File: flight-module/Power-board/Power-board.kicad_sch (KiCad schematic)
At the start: 22 parts, among them J1 POWER, J3 XT60-M, J5 POWER, J8 XT60-M, U1 AZ1117IH-3.3TRG1, U4 AZ1117IH-5TRG1

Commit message: Added a gpio expander to power board.
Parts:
- added J2, J4, J6: Conn_01x02_Male, Connector_PinHeader_2.54mm:PinHeader_1x02_P2.54mm_Vertical, symbol Connector:Conn_01x02_Male
- added R21, R22, R23: 10k, Resistor_SMD:R_0603_1608Metric, symbol Device:R_Small
- added U2: PCF8575DW, PCF8575DW:SOIC127P1030X265-24N, symbol PCF8575DW:PCF8575DW
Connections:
- net +5V: now also U2.24 (VCC)
- net 3.3V: now also J2.1 (Pin_1), J4.1 (Pin_1), J6.1 (Pin_1)
- net GND: now also R21.1, R22.1, R23.1, U2.12 (GND)
- new net: J2.2 (Pin_2), R21.2, U2.2 (A1)
- new net: J4.2 (Pin_2), R22.2, U2.3 (A2)
- new net: J6.2 (Pin_2), R23.2, U2.21 (A0)
- new net I2C_SCL: U2.22 (SCL)
- new net I2C_SDA: U2.23 (SDA)
- new net PYRO10EN: U2.7 (P03)
- new net PYRO1EN: U2.13 (P10)
- new net PYRO2EN: U2.11 (P07)
- new net PYRO3EN: U2.14 (P11)
- new net PYRO4EN: U2.10 (P06)
- new net PYRO5EN: U2.15 (P12)
- new net PYRO6EN: U2.9 (P05)
- new net PYRO7EN: U2.16 (P13)
- new net PYRO8EN: U2.8 (P04)
- new net PYRO9EN: U2.17 (P14)
- no-connect marks 2 -> 9
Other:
- note added: "Connect to LiPo Battery"
- note removed: "Connect to Battery/ Power Supply"
- moved on the sheet: J?A, J?B

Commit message: power board updated
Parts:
- added C8, C9: 22 µF, symbol Device:C
- added D17, D18, D19, D20: D_Schottky, symbol Device:D_Schottky
- added R24, R26: R, symbol Device:R
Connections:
- net 3.3V is gone; now on net +3.3V: C1.2, F2.2, J2.1 (Pin_1), J4.1 (Pin_1), J6.1 (Pin_1)
- net 5V is gone; now on net +5V: C3.2, F3.2
- net BAT2_- is gone; now on net GND2: C4.1, D1.2 (A), J1.2 (Pin_2), J3.N (NEG)
- net +3.3V: now also J?.A1 (Pin_1), J?.A2 (Pin_2)
- net +5V: now also J?.A5 (Pin_5), J?.A6 (Pin_6), J?.A7 (Pin_7), J?.A8 (Pin_8)
- net BAT2_+: now also D19.2 (A)
- net GND2: now reaches J?.A10 (Pin_10)
- net GND2: now also J?.A13 (Pin_13), J?.A14 (Pin_14), J?.A17 (Pin_17), J?.A18 (Pin_18), J?.A21 (Pin_21), J?.A22 (Pin_22), J?.A25 (Pin_25), J?.A26 (Pin_26), J?.A3 (Pin_3), J?.A33 (Pin_33), J?.A34 (Pin_34), J?.A4 (Pin_4), J?.A9 (Pin_9)
- net LOX_Vent: now reaches J?.A11 (Pin_11)
- net LOX_Vent: now also J?.A12 (Pin_12)
- net ETH_Vent: now reaches J?.A15 (Pin_15)
- net ETH_Vent: now also J?.A16 (Pin_16)
- net ETH_Main: now reaches J?.A19 (Pin_19)
- net ETH_Main: now also J?.A20 (Pin_20)
- net PYRO_EX: now reaches J?.A23 (Pin_23)
- net PYRO_EX: now also J?.A24 (Pin_24)
- net Ext_Sup1: now reaches J?.A27 (Pin_27)
- net Ext_Sup1: now also J?.A28 (Pin_28), J?.A29 (Pin_29), J?.A30 (Pin_30), J?.A31 (Pin_31), J?.A32 (Pin_32), D17.2 (A)
- net Ext_Sup2: now reaches J?.A35 (Pin_35)
- net Ext_Sup2: now also J?.A36 (Pin_36), J?.A37 (Pin_37), J?.A38 (Pin_38), J?.A39 (Pin_39), J?.A40 (Pin_40), D20.2 (A)
- net 12V renamed V_sensor_+
- net V_sensor_+: now also D18.1 (K), R26.2; no longer F1.2
- net PYRO10EN: no longer names the net of U2.7 (P03)
- net PYRO5EN: no longer names the net of U2.15 (P12)
- net PYRO6EN: no longer names the net of U2.9 (P05)
- net PYRO7EN: no longer names the net of U2.16 (P13)
- net PYRO8EN: no longer names the net of U2.8 (P04)
- net PYRO9EN: no longer names the net of U2.17 (P14)
- new net: C9.1, D20.1 (K)
- new net: C9.2, R24.1
- new net: C8.2, R26.1
- new net: C8.1, D17.1 (K)
- new net BAT1_+: D18.2 (A), F1.2
- new net V_pyro_+: D19.1 (K), R24.2
- no-connect marks 9 -> 15
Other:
- added sheet Pyro 7 (pyro.kicad_sch)
- added sheet Pyro 8 (pyro.kicad_sch)
- added sheet level_shifter (i2c_level_shifter.kicad_sch)
- moved on the sheet: J?A

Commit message: updated power board.
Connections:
- net BAT1_+: now also F1.1; no longer F1.2
- net GND: now also J?.B17 (Pin_17), J?.B25 (Pin_25), J?.B33 (Pin_33), J?.B5 (Pin_5), J?.B9 (Pin_9)
- net I2C_SCL: now also J?.B3 (Pin_3); no longer U2.22 (SCL)
- net I2C_SCL_5V: now also U2.22 (SCL)
- net I2C_SDA: now also J?.B1 (Pin_1); no longer U2.23 (SDA)
- net I2C_SDA_5V: now also U2.23 (SDA)
- net at J?.B14 (Pin_14): now also J?.B20 (Pin_20), J?.B26 (Pin_26), J?.B34 (Pin_34), J?.B8 (Pin_8)
- net BAT1_+_pre: no longer names the net of C6.2, J5.1 (Pin_1), J8.P (POS), R3.1
- net BAT1_+_pre: now also F1.2; no longer F1.1
- net BAT2_+_pre: no longer names the net of C4.2, F4.1, J1.1 (Pin_1), J3.P (POS), R1.1
- no-connect marks 15 -> 43
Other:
- moved on the sheet: C4, C6, D1, D2, F1, F4, J1, J3, J5, J8, J?B, R1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

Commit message: Updated core-board
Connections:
- net V_pyro_+ is gone; now on net +5V: D19.1 (K), R24.2
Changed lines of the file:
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@@
+    (stroke (width 0) (type default))
+  )
+  (wire (pts (xy 238.506 96.266) (xy 238.506 99.06))
     (stroke (width 0) (type default))
   )
@@
     (effects (font (size 1.27 1.27)) (justify right))
     (property "Intersheetrefs" "${INTERSHEET_REFS}" (at 164.4976 162.56 0)
+      (effects (font (size 1.27 1.27)) (justify right) hide)
+    )
+  )
+  (global_label "V_pyro_+" (shape input) (at 238.506 99.06 270) (fields_autoplaced)
+    (effects (font (size 1.27 1.27)) (justify right))
+    (property "Intersheetrefs" "${INTERSHEET_REFS}" (at 238.506 110.6932 90)
       (effects (font (size 1.27 1.27)) (justify right) hide)
     )
@@
         )
       )
+    )
+  )
+  (symbol (lib_id "power:+5V") (at 238.506 96.266 0) (unit 1)
+    (in_bom yes) (on_board yes) (dnp no)
+    (property "Reference" "#PWR011" (at 238.506 100.076 0)
+      (effects (font (size 1.27 1.27)) hide)
+    )
+    (property "Value" "+5V" (at 240.284 91.694 0)
+      (effects (font (size 1.27 1.27)))
+    )
+    (property "Footprint" "" (at 238.506 96.266 0)
+      (effects (font (size 1.27 1.27)) hide)
+    )
+    (property "Datasheet" "" (at 238.506 96.266 0)
+      (effects (font (size 1.27 1.27)) hide)
+    )
+    (pin "1")
+    (instances
+      (project "Power-board"
+        (path "/9e0a4b39-2b30-4bec-9684-92acf902e3a8"
+          (reference "#PWR011") (unit 1)
+        )
+      )

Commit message: update on flight pcbs
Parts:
- removed D1, D2: D_Small, Diode_SMD:D_0603_1608Metric, symbol Device:D_Small
- added D1, D2: D_Schottky, symbol Device:D_Schottky
- gave numbers to parts that had none: 1
- renumbered C4 to C1, C6 to C2, C2 to C3, C5 to C4, C8 to C5, C9 to C6, C1 to C7, C3 to C8, D18 to D3, D19 to D4, D17 to D5, D20 to D6, F4 to F2, F2 to F3, F3 to F4, J5 to J1, J1 to J2, J8 to J4, J2 to J6, J4 to J7, J6 to J8, R3 to R2, R26 to R3, R24 to R4, R21 to R5, R22 to R6, R23 to R7, U4 to U2, U2 to U3
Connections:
- net GND: now also D2.2 (A)
- net GND2: now also D1.2 (A)
- net at R2.2: now also D2.1 (K)
- net at R1.2: now also D1.1 (K)
- net ETH_Main: no longer names the net of J5.A19 (Pin_19)
- net ETH_Main: no longer J5.A20 (Pin_20)
- net PYRO3EN: no longer names the net of U3.14 (P11)
- net PYRO4EN: no longer names the net of U3.10 (P06)
- net PYRO_EX: no longer names the net of J5.A23 (Pin_23)
- net PYRO_EX: no longer J5.A24 (Pin_24)
- no-connect marks 43 -> 49
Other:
- removed sheet Pyro 5
- removed sheet Pyro 6
- removed sheet Pyro 7
- removed sheet Pyro 8

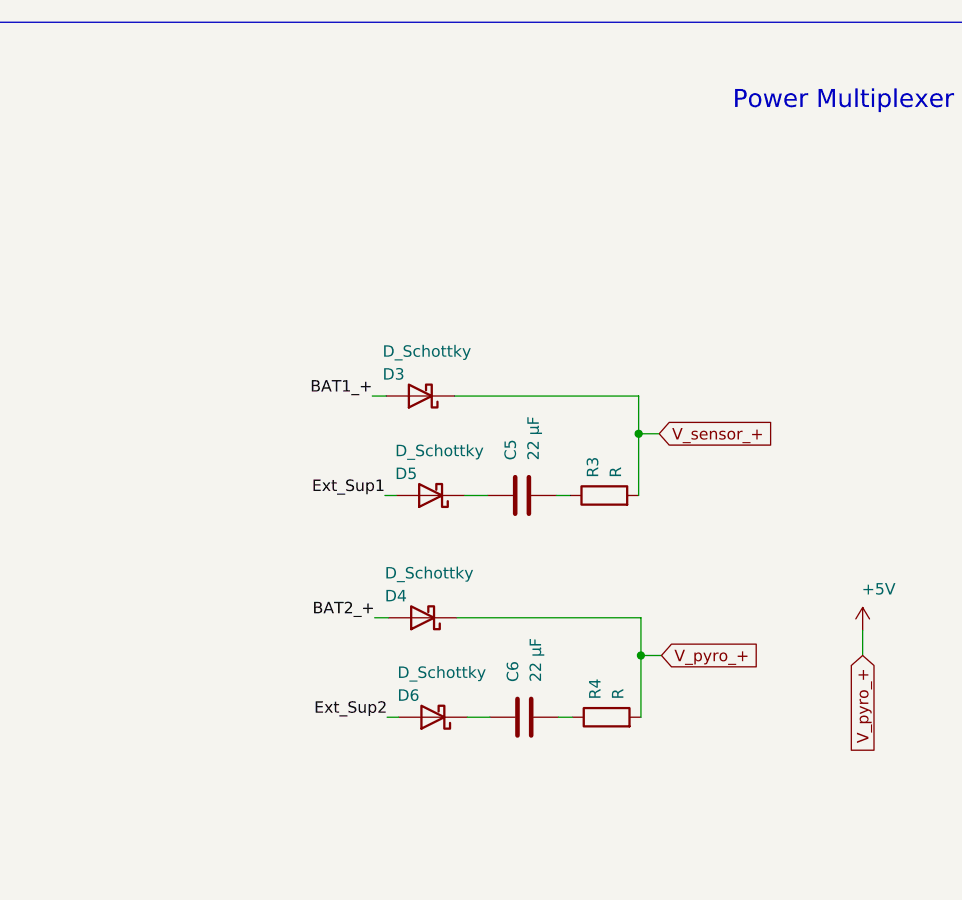
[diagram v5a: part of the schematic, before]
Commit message: Updated power mux circuit.
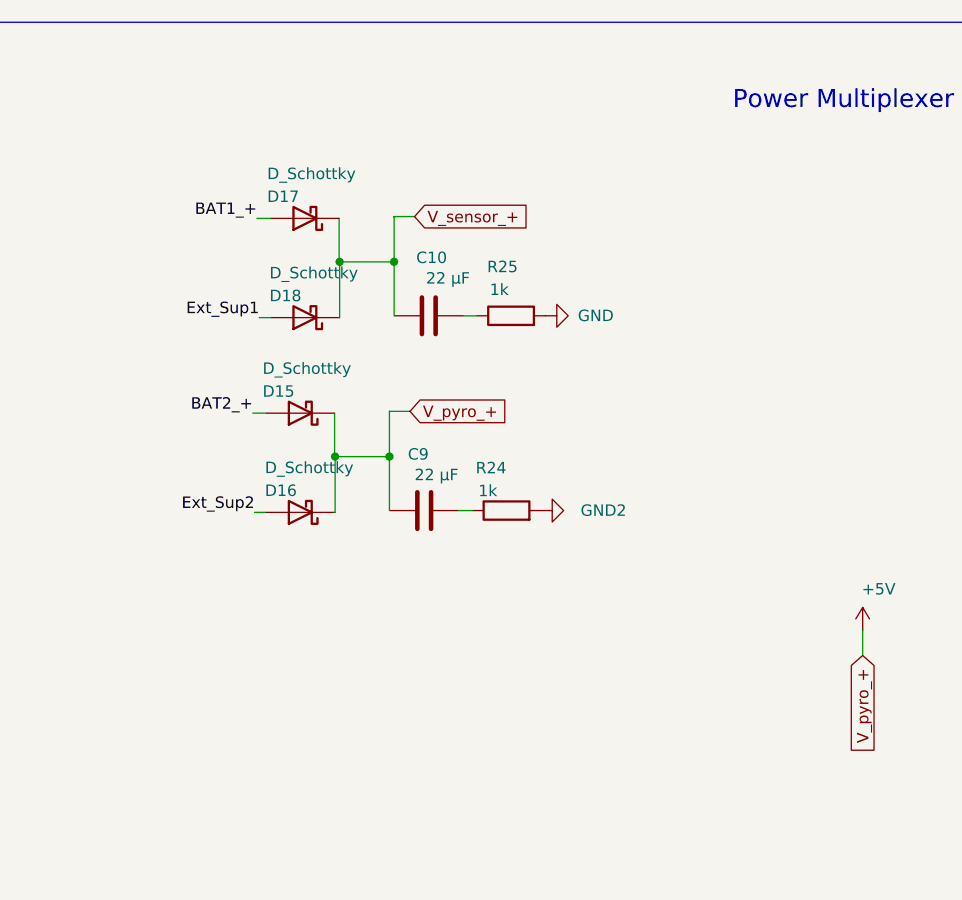
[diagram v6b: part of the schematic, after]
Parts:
- removed C5, C6: 22 µF, symbol Device:C
- removed D3, D4, D5, D6: D_Schottky, symbol Device:D_Schottky
- removed R3, R4: R, symbol Device:R
- added C10, C9: 22 µF, symbol Device:C
- added D15, D16, D17, D18: D_Schottky, symbol Device:D_Schottky
- added R24, R25: 1k, symbol Device:R
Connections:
- net +5V: now also D15.1 (K), D16.1 (K)
- net BAT1_+: now also D17.2 (A)
- net BAT2_+: now also D15.2 (A)
- net Ext_Sup1: now also D18.2 (A)
- net Ext_Sup2: now also D16.2 (A)
- net GND: now also R25.2
- net GND2: now also R24.2
- net V_sensor_+: now also D17.1 (K), D18.1 (K)
- new net: C10.2, R25.1
- new net: C9.2, R24.1
